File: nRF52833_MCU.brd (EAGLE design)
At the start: 51.3 x 30.2 mm, 49 parts, among them IC1 SKY13415-485LF, J1 282834-2, J100 DEBUG_CONNECTOR, J2 282834-2, J3 282834-2, U1 nRF52833-QIAA, U3 BQ25570RGRR, X1 32MHz, X2 32.768kHz, X3 22-23-2031

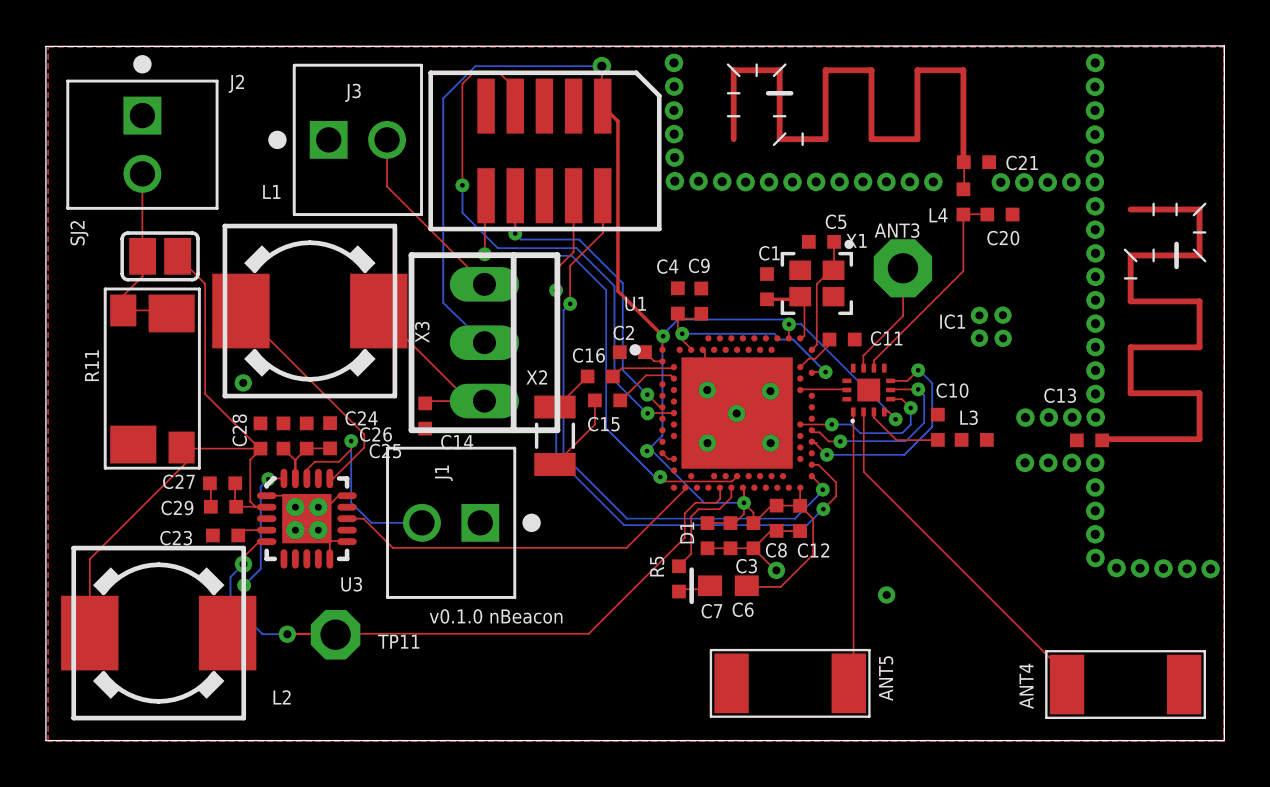
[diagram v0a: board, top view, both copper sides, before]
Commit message: Routing the antennas
Signed-off-by: Florian Depraz <florian.depraz@outlook.com>
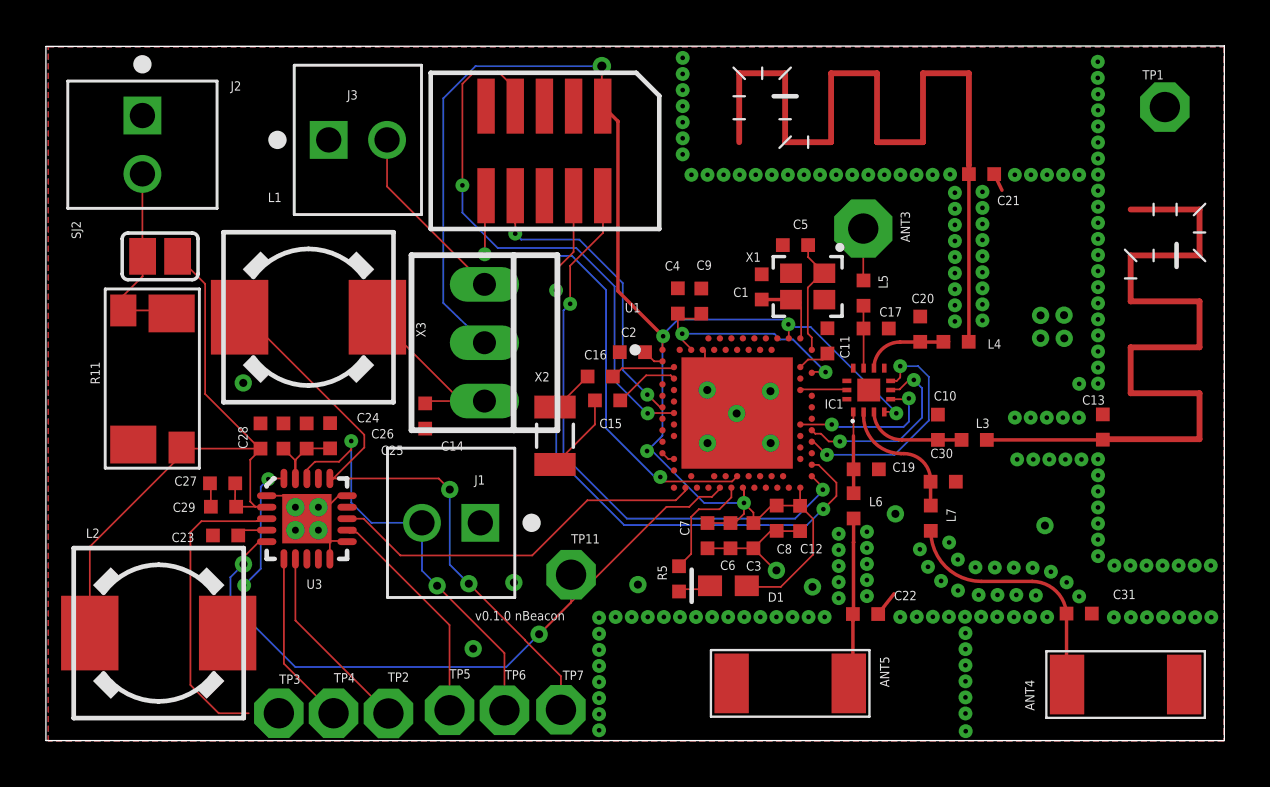
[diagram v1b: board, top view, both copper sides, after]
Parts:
- added C17, C19, C30: 0.7pF, Nordic_misc:RESC0402_N
- added C22, C31: N.C., Nordic_misc:RESC0402_N
- added L5, L6, L7: 2.2nH, Nordic_misc:RESC0402_N
- added TP1, TP2, TP3, TP4, TP5, TP6, TP7: TPPAD1-13, testpad:P1-13
- moved TP11 10.6 mm to (25.8, 9.63)
- moved L4 6.10 mm to (42.6, 19.8), turned to 0 degrees
- moved C20 6.08 mm to (41.0, 20.3), turned to 90 degrees
- moved ANT3 2.45 mm to (38.5, 24.7)
- moved C5 1.14 mm to (35.6, 24.0)
- moved C13 0.82 mm to (49.0, 16.1), turned to 90 degrees
- moved C11 0.64 mm to (37.0, 19.8), turned to 90 degrees
- moved C21 0.56 mm to (43.7, 27.1)
- moved X1 0.42 mm to (36.1, 22.2)
- moved L1 0.28 mm to (14.4, 20.8)
- moved ANT2 0.27 mm to (43.1, 27.5)
- moved C1 0.23 mm to (34.1, 22.2)
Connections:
- new net N$12: ANT3.1, L5.2
- new net N$13: ANT5.1, C22.1, L6.2
- new net N$14: ANT4.1, C31.1, L7.2
- new net N$18: TP1.TP
- net ANT_OUT_RF3: now also C30.1, L7.1; no longer ANT4.1
- net ANT_OUT_RF4: now also C17.1, L5.1; no longer ANT3.1
- net ANT_OUT_RF5: now also C19.1, L6.1; no longer ANT5.1
- net BQ_EXT_VBAT: now also TP6.TP
- net BQ_LBUCK: now also TP7.TP
- net BQ_VBAT_OV: now also TP2.TP
- net BQ_VOUT_EN: now also TP4.TP
- net BQ_VOUT_SET: now also TP5.TP
- net GND: now also C17.2, C19.2, C22.2, C30.2, C31.2
- net VOC_SAMP: now also TP3.TP
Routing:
- net BQ_LBUCK: track 10.2 -> 27.2 mm, vias 0 -> 2
- net VOC_SAMP: track 0.10 -> 13.3 mm
- net N$14: track 0.00 -> 10.5 mm, vias 1 -> 0
- net ANT_OUT_RF3: track 15.5 -> 5.50 mm
- net BQ_VOUT_SET: track 0.00 -> 9.88 mm
- net BQ_EXT_VBAT: track 9.17 -> 18.8 mm, vias 1 -> 2
- net BQ_VBAT_OV: track 0.00 -> 8.41 mm
- net ANT_OUT_RF5: track 11.9 -> 3.55 mm
- net BQ_VOUT_EN: track 0.00 -> 7.61 mm
- net N$13: track 0.00 -> 7.56 mm
- net N$40: track 1.25 -> 7.34 mm
- net ANT_OUT_RF2: track 9.34 -> 4.13 mm
- net N$5: track 0.00 -> 5.16 mm
- net ANT_OUT_RF4: track 5.07 -> 2.79 mm
- net N$12: track 0.00 -> 2.26 mm, vias 1 -> 0
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
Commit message: Add pcb trace antenna 0.7mm
Signed-off-by: Florian Depraz <florian.depraz@outlook.com>
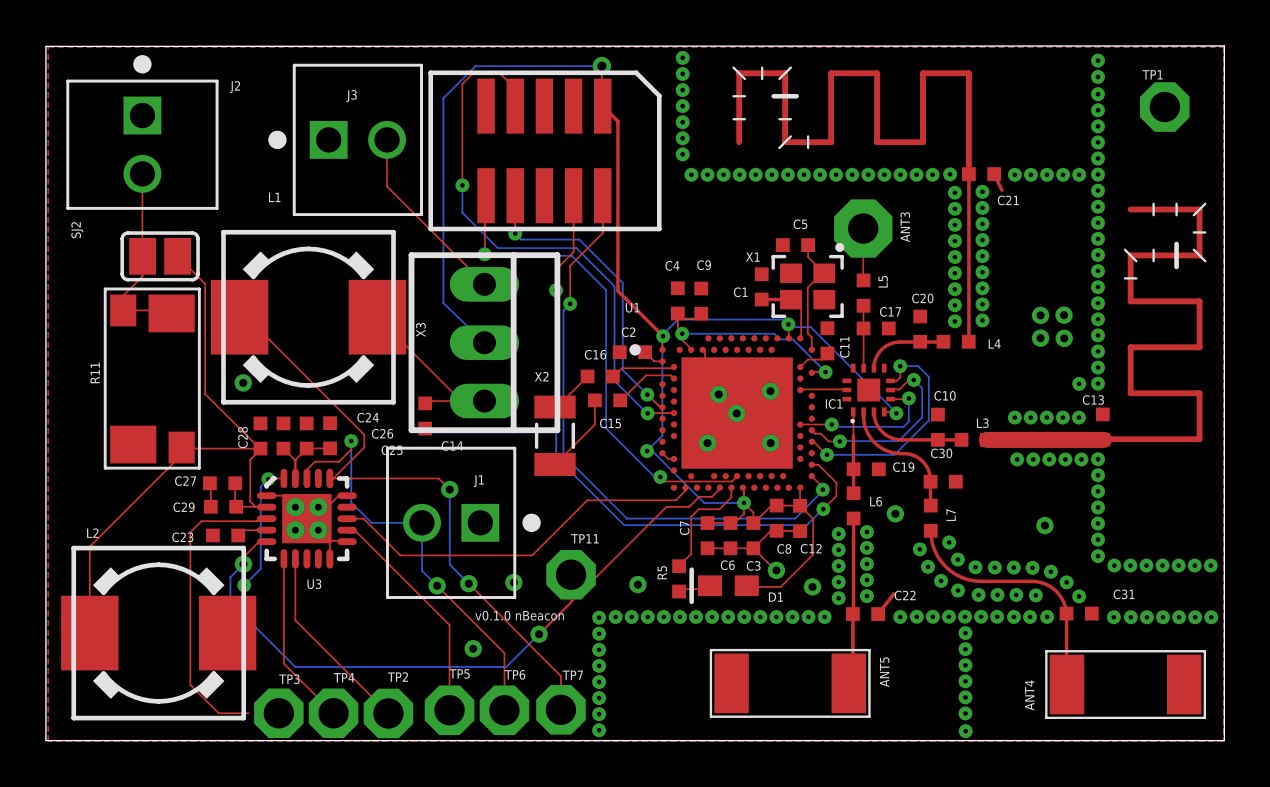
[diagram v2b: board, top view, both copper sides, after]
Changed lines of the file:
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@@
 <rectangle x1="33.605" y1="-3.675" x2="38.605" y2="13.515" layer="42" rot="R90"/>
 <rectangle x1="41.51" y1="14.36" x2="44.8" y2="16.09" layer="41"/>
-<rectangle x1="42.75" y1="16.1" x2="45.19" y2="16.74" layer="41"/>
 <rectangle x1="37.66" y1="11.57" x2="38.64" y2="14.72" layer="41"/>
-<rectangle x1="38.56" y1="11.57" x2="39.05" y2="13.67" layer="41"/>
+<rectangle x1="40.56" y1="18.49" x2="43.85" y2="20.22" layer="41"/>
 </plain>
 <attributes>
@@
 <wire x1="49.02996875" y1="15.50996875" x2="48.98" y2="15.51" width="0.1524" layer="1"/>
 <contactref element="C13" pad="1"/>
-<wire x1="43.93" y1="15.5" x2="49.02996875" y2="15.5" width="0.1524" layer="1"/>
+<wire x1="43.93" y1="15.5" x2="49.02996875" y2="15.5" width="0.7" layer="1"/>
 <wire x1="49.02996875" y1="15.5" x2="49.02996875" y2="15.50996875" width="0.1524" layer="1"/>
 <wire x1="48.98" y1="15.51" x2="49.19" y2="15.53" width="0" layer="19" extent="1-1"/>
@@
 <via x="46.54" y="16.47" extent="1-16" drill="0.2"/>
 <via x="45.84" y="16.47" extent="1-16" drill="0.2"/>
-<wire x1="48.77" y1="29.85" x2="48.77" y2="30.55" width="0" layer="19" extent="1-1"/>
+<wire x1="48.77" y1="30.55" x2="48.77" y2="29.85" width="0" layer="19" extent="1-1"/>
 <wire x1="48.77" y1="29.15" x2="48.77" y2="29.85" width="0" layer="19" extent="1-1"/>
 <wire x1="48.77" y1="28.45" x2="48.77" y2="29.15" width="0" layer="19" extent="1-1"/>
@@
 <via x="11.56" y="17.98" extent="1-16" drill="0.35"/>
 <via x="31.77" y="15.36" extent="1-16" drill="0.35"/>
-<via x="31.76" y="17.67" extent="1-16" drill="0.35"/>
+<via x="32.26" y="17.48" extent="1-16" drill="0.35"/>
 <via x="34.51" y="17.62" extent="1-16" drill="0.35"/>
 <via x="34.52" y="15.36" extent="1-16" drill="0.35"/>
@@
 <wire x1="39.2" y1="7.92" x2="39.89" y2="8.8" width="0.1524" layer="1"/>
 <wire x1="44.25" y1="27.07" x2="44.59" y2="26.37" width="0.1524" layer="1"/>
-<wire x1="31.76" y1="17.67" x2="32.2725" y2="17.4575" width="0" layer="19" extent="1-1"/>
+<wire x1="32.26" y1="17.48" x2="32.2725" y2="17.4575" width="0" layer="19" extent="1-1"/>
 <wire x1="14.83" y1="13.82" x2="14.83" y2="12.57" width="0" layer="19" extent="1-1"/>
 <wire x1="14.83" y1="10.32" x2="14.83" y2="11.57" width="0" layer="19" extent="1-1"/>
@@
 </signal>
 <signal name="N$11">
-<via x="48.76" y="31.26" extent="1-16" drill="0.2"/>
-<via x="48.76" y="31.96" extent="1-16" drill="0.2"/>
-<wire x1="48.76" y1="31.96" x2="48.76" y2="31.26" width="0" layer="19" extent="1-1"/>
+<via x="48.77" y="31.3" extent="1-16" drill="0.2"/>
+<via x="48.77" y="32.01" extent="1-16" drill="0.2"/>
+<wire x1="48.77" y1="32.01" x2="48.77" y2="31.3" width="0" layer="19" extent="1-1"/>
 </signal>
 <signal name="N$12">
@@
 <wire x1="38.1" y1="7.92" x2="38.1" y2="5.08" width="0.1524" layer="1"/>
 <wire x1="38.1" y1="5.08" x2="37.92" y2="4.9" width="0.1524" layer="1"/>
-<via x="38.71" y="11.5" extent="1-16" drill="0.2" alwaysstop="yes"/>
+<via x="38.71" y="11.49" extent="1-16" drill="0.2" alwaysstop="yes"/>
 <wire x1="38.13" y1="12.08" x2="38.13" y2="11.0464625" width="0.1524" layer="1"/>
 <wire x1="38.1256125" y1="11.042075" x2="38.1256125" y2="7.9456125" width="0.1524" layer="1"/>
 <wire x1="38.1" y1="7.92" x2="38.1256125" y2="7.9456125" width="0.1524" layer="1"/>
 <wire x1="38.13" y1="11.0464625" x2="38.1256125" y2="11.042075" width="0.1524" layer="1"/>
-<wire x1="38.13" y1="12.08" x2="38.71" y2="11.5" width="0" layer="19" extent="1-1"/>
+<wire x1="38.13" y1="12.08" x2="38.71" y2="11.49" width="0" layer="19" extent="1-1"/>
 </signal>
 <signal name="N$14">
